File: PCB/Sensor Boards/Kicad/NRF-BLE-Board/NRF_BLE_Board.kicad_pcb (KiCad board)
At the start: 2 copper layers, 5.7 x 5.7 mm, 13 parts, among them U1 nRF52805-CAxx, Y1 Crystal

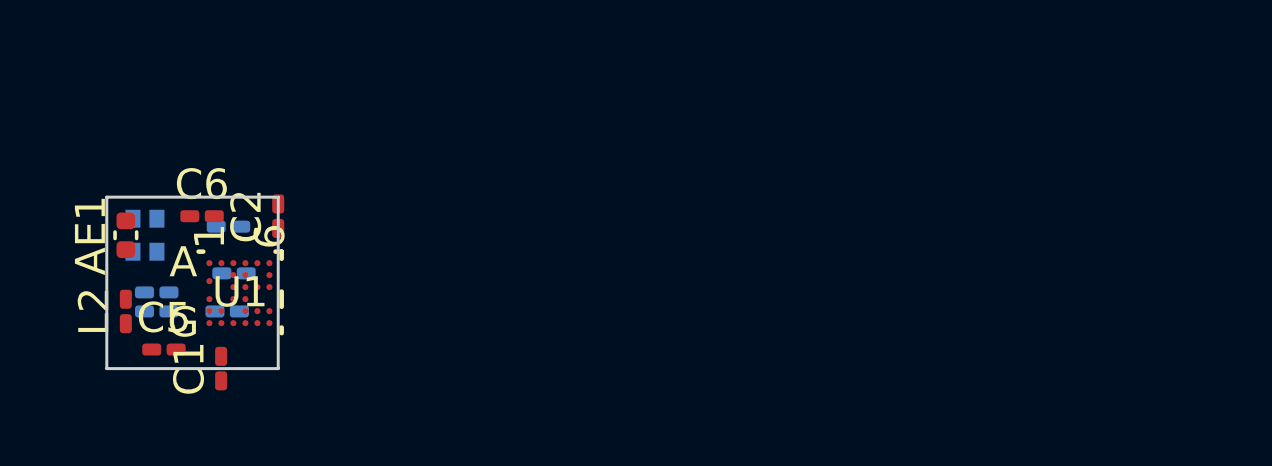
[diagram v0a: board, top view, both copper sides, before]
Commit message: Initial placement and routing done
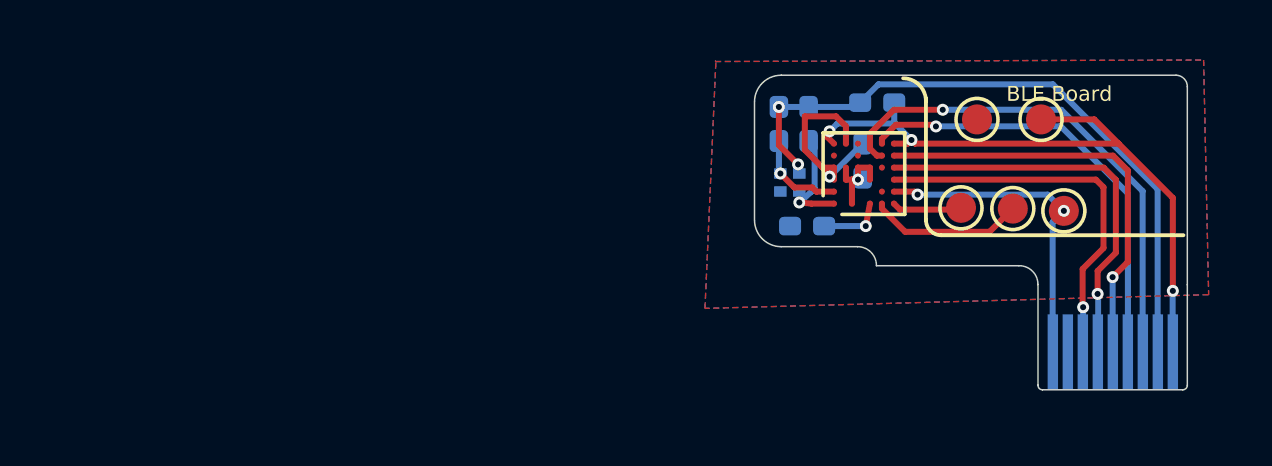
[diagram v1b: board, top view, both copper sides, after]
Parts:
- removed C3, C5, C7, C8: C, Capacitor_SMD:C_0201_0603Metric_Pad0.64x0.40mm_HandSolder
- removed L1, L2: INDUCTOR, Inductor_SMD:L_0201_0603Metric_Pad0.64x0.40mm_HandSolder
- removed Y1: Crystal, Oscillator:Oscillator_SMD_Abracon_ASCO-4Pin_1.6x1.2mm
- added TP1: TestPoint, TestPoint:TestPoint_Pad_D1.0mm, F.Cu at (170.2, 90.8)
- added TP2: TestPoint, TestPoint:TestPoint_Pad_D1.0mm, F.Cu at (168.1, 90.8)
- added TP3: TestPoint, TestPoint:TestPoint_Pad_D1.0mm, F.Cu at (171.0, 93.8)
- added TP4: TestPoint, TestPoint:TestPoint_Pad_D1.0mm, F.Cu at (167.5, 93.7)
- added TP5: TestPoint, TestPoint:TestPoint_Pad_D1.0mm, F.Cu at (169.3, 93.7)
- added U$1: FH19C-9S-0.5SH_10-FFC, OSO-SWAB-B1-00 Sensor Watch Accelerometer:FH19C9S05SH10-FFC, F.Cu at (172.6, 96.3)
- added Y2: 32MHz, Crystal:Crystal_SMD_Murata_XRCTD32M000N1P1AR0-4pin_1.2x1.0mm, B.Cu at (161.8, 92.9)
- AE1: footprint Capacitor_SMD:C_0402_1005Metric -> Capacitor_SMD:C_0402_1005Metric_Pad0.74x0.62mm_HandSolder; moved to B.Cu
- C1, C2: footprint Capacitor_SMD:C_0201_0603Metric_Pad0.64x0.40mm_HandSolder -> Capacitor_SMD:C_0402_1005Metric_Pad0.74x0.62mm_HandSolder; moved to B.Cu
- C4: value C -> 1uF; footprint Capacitor_SMD:C_0201_0603Metric_Pad0.64x0.40mm_HandSolder -> Capacitor_SMD:C_0402_1005Metric_Pad0.74x0.62mm_HandSolder
- C6: value C -> 1uF; footprint Capacitor_SMD:C_0201_0603Metric_Pad0.64x0.40mm_HandSolder -> Capacitor_SMD:C_0402_1005Metric_Pad0.74x0.62mm_HandSolder; moved to B.Cu
- U1: footprint Package_CSP:NRF_WLCSP-28_2.482X2.464_NOR -> Package_CSP:NRF_WLCSP-28_2.48x2.64mm_P0.4mm
- moved AE1 22.7 mm to (162.4, 94.3), turned to 180 degrees
- moved C4 22.2 mm to (164.7, 90.2)
- moved C6 22.1 mm to (164.3, 92.1), turned to -90 degrees
- moved C1 21.2 mm to (162.5, 90.9), turned to -90 degrees
- moved U1 21.2 mm to (164.3, 92.6), turned to 90 degrees
- moved C2 17.0 mm to (161.5, 90.9), turned to -90 degrees
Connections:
- C4 pad 1: Net-(C4-Pad1) -> VCC
- U1 pad A3: Net-(U1-DEC2) -> Net-(U1-DEC1)
- U1 pad A4: Net-(U1-DEC2) -> Net-(U1-DEC1)
- U1 pad A6: Net-(C4-Pad1) -> VCC
- U1 pad C1: Net-(U1-DEC1) -> GND
- U1 pad E1: Net-(U1-ANT) -> Net-(AE1-A)
- U1 pad F1: unconnected-(U1-SWDIO-PadF1) -> Net-(U1-SWDIO)
- U1 pad F5: unconnected-(U1-P0.04/AIN2-PadF5) -> /GPIO1
- U1 pad F6: unconnected-(U1-P0.05/AIN3-PadF6) -> /GPIO0
- U1 pad G1: unconnected-(U1-SWDCLK-PadG1) -> Net-(U1-SWDCLK)
- U1 pad G2: unconnected-(U1-P0.21/nRESET-PadG2) -> /nReset
- U1 pad G3: unconnected-(U1-P0.18-PadG3) -> /GPIO4
- U1 pad G4: unconnected-(U1-P0.16-PadG4) -> /GPIO3
- U1 pad G5: unconnected-(U1-P0.12-PadG5) -> /GPIO2
- U1 pad G6: Net-(C7-Pad1) -> VCC
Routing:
- net GND: track 0.00 -> 25.3 mm, vias 0 -> 3
- net VCC: track 0.00 -> 22.6 mm, vias 0 -> 3
- net /GPIO1: track 0.00 -> 16.9 mm, vias 0 -> 1
- net /GPIO0: track 0.00 -> 14.8 mm, vias 0 -> 1
- net /GPIO2: track 0.00 -> 14.3 mm, vias 0 -> 1
- net /GPIO3: track 0.00 -> 13.6 mm, vias 0 -> 1
- net /GPIO4: track 0.00 -> 12.9 mm, vias 0 -> 1
- net /nReset: track 0.00 -> 10.8 mm, vias 0 -> 2
- net Net-(U1-DEC1): track 0.00 -> 6.78 mm, vias 0 -> 1
- net Net-(U1-SWDIO): track 0.00 -> 5.17 mm
- net Net-(U1-XC1): track 0.00 -> 3.51 mm, vias 0 -> 1
- net Net-(U1-XC2): track 0.00 -> 3.14 mm, vias 0 -> 1
- net Net-(U1-SWDCLK): track 0.00 -> 2.34 mm
- net Net-(AE1-A): track 0.00 -> 2.15 mm, vias 0 -> 1
- added copper zone on B.Cu, net GND
- added copper zone on F.Cu, net GND
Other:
- board size 5.7 x 5.7 mm -> 14.4 x 10.5 mm
- board text added: "BLE Board"

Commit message: Routing completed
order placed at OSH Park with this gerber.
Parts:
- removed TP1, TP2, TP4, TP5: TestPoint, TestPoint:TestPoint_Pad_D1.0mm
- added J1: Conn_01x04, TestPoint:TestPoint_4Pads_Pitch1.27mm, F.Cu at (171.3, 93.7)
- moved TP3 3.48 mm to (167.5, 93.7)
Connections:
- U1 pad F1: Net-(U1-SWDIO) -> /SWDIO
- U1 pad G1: Net-(U1-SWDCLK) -> /SWDCLK
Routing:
- net GND: track 25.3 -> 35.2 mm, vias 3 -> 4
- net /SWDIO: track 0.00 -> 6.31 mm
- net Net-(U1-SWDIO): track 5.17 -> 0.00 mm
- net /SWDCLK: track 0.00 -> 4.21 mm
- net /GPIO2: track 14.3 -> 11.3 mm
- net /GPIO3: track 13.6 -> 10.6 mm
- net /GPIO4: track 12.9 -> 9.93 mm
- net Net-(U1-SWDCLK): track 2.34 -> 0.00 mm
- net /nReset: track 10.8 -> 8.81 mm, vias 2 -> 1
- net /GPIO0: track 14.8 -> 13.1 mm
- net /GPIO1: track 16.9 -> 15.3 mm
- net VCC: track 22.6 -> 23.4 mm
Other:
- board text added: "GND"
- board text added: "NRF BLE Board"
- board text added: "SCLK"
- board text added: "SDIO"
- board text added: "VCC"
- board text removed: "BLE Board"
